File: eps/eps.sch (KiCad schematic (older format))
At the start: 10 parts, among them Q18 IRLZ44N, U4 STM32F411CEUx, U5 LTC4365TS8

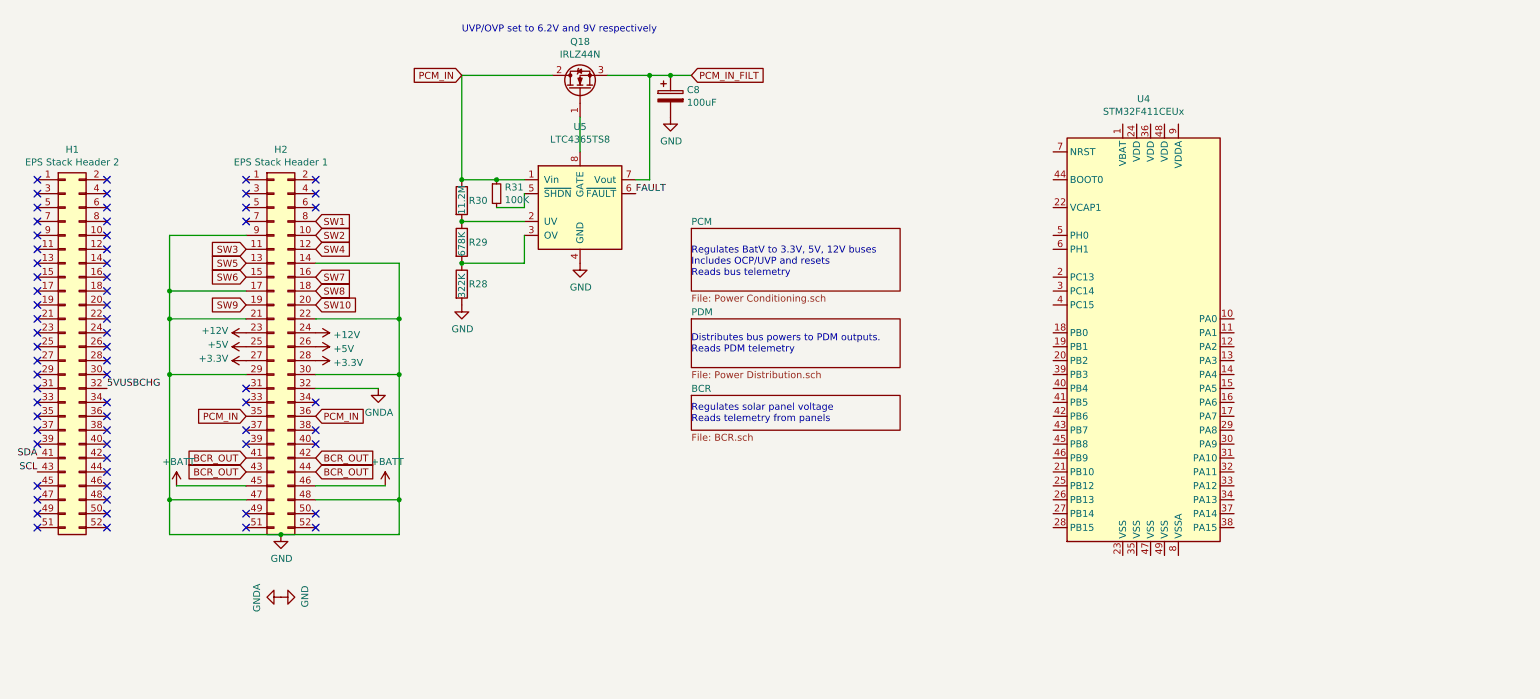
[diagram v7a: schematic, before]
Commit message: current limiters
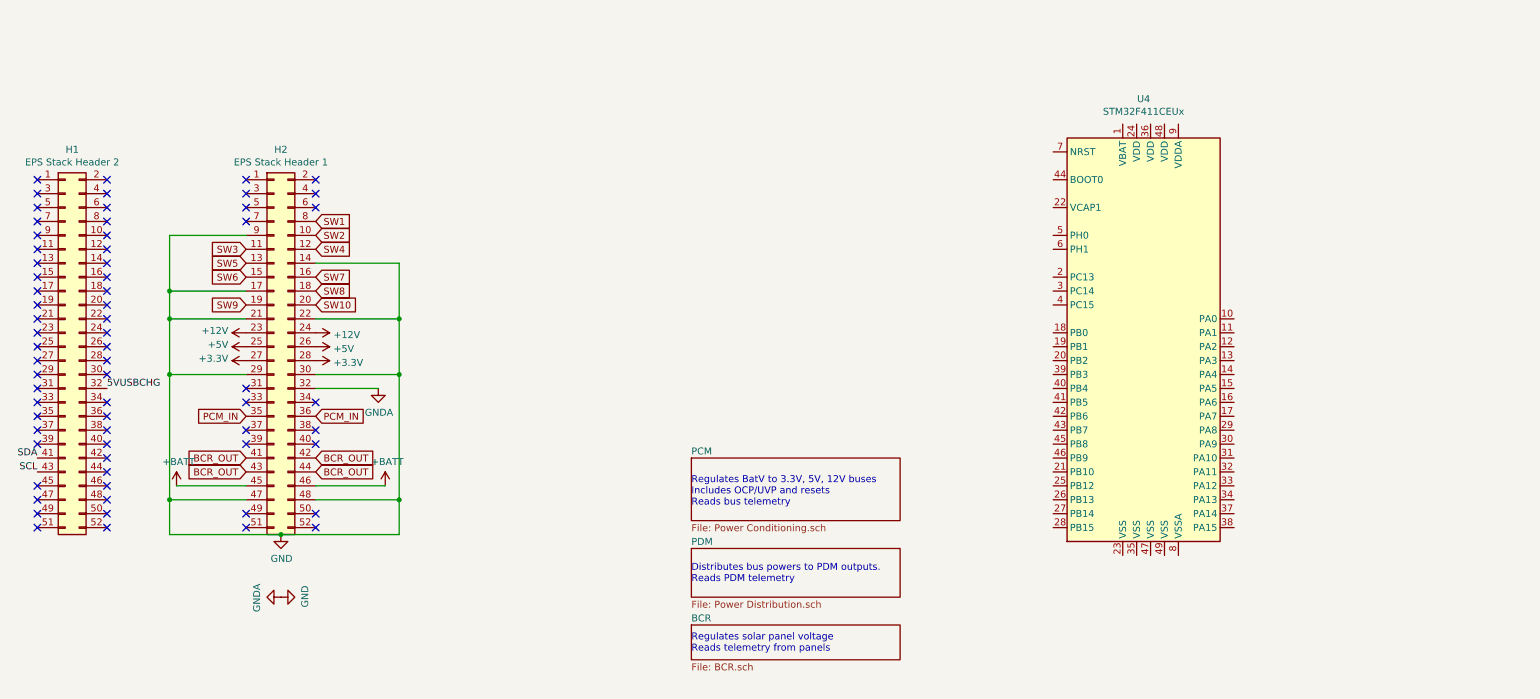
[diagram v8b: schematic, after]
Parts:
- removed C8: 100uF, symbol Device:CP
- removed Q18: IRLZ44N, Package_TO_SOT_THT:TO-220-3_Vertical, symbol Transistor_FET:IRLZ44N
- removed R28: 322K, symbol Device:R
- removed R29: 678K, symbol Device:R
- removed R30: 11.2M, symbol Device:R
- removed R31: 100K, symbol Device:R_Small
- removed U5: LTC4365TS8, symbol Power_Management:LTC4365TS8
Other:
- note removed: "UVP/OVP set to 6.2V and 9V respectively"
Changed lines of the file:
@@
 $EndComp
 $Sheet
-S 5450 2000 1500 450
+S 5450 3650 1500 450
 U 619279C9
 F0 "PCM" 50
@@
 $EndSheet
 $Sheet
-S 5450 2650 1500 350
+S 5450 4300 1500 350
 U 61928B56
 F0 "PDM" 50
@@
 $EndSheet
 $Sheet
-S 5450 3200 1500 250
+S 5450 4850 1500 250
 U 61929CC0
 F0 "BCR" 50
@@
 Text GLabel 2750 1950 2    50   Input ~ 0
 SW1
-Text Notes 5450 2350 0    50   ~ 0
+Text Notes 5450 4000 0    50   ~ 0
 Regulates BatV to 3.3V, 5V, 12V buses\nIncludes OCP/UVP and resets\nReads bus telemetry
-Text Notes 5450 2900 0    50   ~ 0
+Text Notes 5450 4550 0    50   ~ 0
 Distributes bus powers to PDM outputs. \nReads PDM telemetry\n
-Text Notes 5450 3400 0    50   ~ 0
+Text Notes 5450 5050 0    50   ~ 0
 Regulates solar panel voltage\nReads telemetry from panels\n
 $Comp
@@
 	1    0    0    -1
 $EndComp
-$Comp
-L Power_Management:LTC4365TS8 U5
-U 1 1 6180BC68
-P 4650 1850
-F 0 "U5" H 4650 2431 50  0000 C CNN
-F 1 "LTC4365TS8" H 4650 2340 50  0000 C CNN
-F 2 "" H 4350 2100 50  0001 C CNN
-F 3 "https://www.analog.com/media/en/technical-documentation/data-sheets/4365fa.pdf" H 4650 1950 50  0001 C CNN
-	1    4650 1850
-	1    0    0    -1
-$EndComp
-$Comp
-L Transistor_FET:IRLZ44N Q18
-U 1 1 6180D601
-P 4650 1000
-F 0 "Q18" V 4992 1000 50  0000 C CNN
-F 1 "IRLZ44N" V 4901 1000 50  0000 C CNN
-F 2 "Package_TO_SOT_THT:TO-220-3_Vertical" H 4900 925 50  0001 L CIN
-F 3 "http://www.irf.com/product-info/datasheets/data/irlz44n.pdf" H 4650 1000 50  0001 L CNN
-	1    4650 1000
-	0    -1   -1   0
-$EndComp
-Wire Wire Line
-	4650 1450 4650 1200
-Text GLabel 3800 900  0    50   Input ~ 0
-PCM_IN
-Wire Wire Line
-	3800 1650 3800 900
-Wire Wire Line
-	4850 900  5150 900
-Wire Wire Line
-	5050 1650 5150 1650
-Wire Wire Line
-	5150 1650 5150 900
-Text GLabel 5450 900  2    50   Input ~ 0
-PCM_IN_FILT
-Wire Wire Line
-	5150 900  5300 900
-Connection ~ 5150 900
-$Comp
-L Device:CP C8
-U 1 1 618175DC
-P 5300 1050
-F 0 "C8" H 5418 1096 50  0000 L CNN
-F 1 "100uF" H 5418 1005 50  0000 L CNN
-F 2 "" H 5338 900 50  0001 C CNN
-F 3 "~" H 5300 1050 50  0001 C CNN
-	1    5300 1050
-	1    0    0    -1
-$EndComp
-Connection ~ 5300 900
-Wire Wire Line
-	5300 900  5450 900
-$Comp
-L power:GND #PWR033
-U 1 1 6181B18B
-P 5300 1200
-F 0 "#PWR033" H 5300 950 50  0001 C CNN
-F 1 "GND" H 5305 1027 50  0000 C CNN
-F 2 "" H 5300 1200 50  0001 C CNN
-F 3 "" H 5300 1200 50  0001 C CNN
-	1    5300 1200
-	1    0    0    -1
-$EndComp
-$Comp
-L Device:R R28
-U 1 1 6181BFCB
-P 3800 2400
-F 0 "R28" H 3850 2400 50  0000 L CNN
-F 1 "322K" V 3800 2300 50  0000 L CNN
-F 2 "" V 3730 2400 50  0001 C CNN
-F 3 "~" H 3800 2400 50  0001 C CNN
-	1    3800 2400
-	1    0    0    -1
-$EndComp
-$Comp
-L Device:R R29
-U 1 1 6181C3B8
-P 3800 2100
-F 0 "R29" H 3850 2100 50  0000 L CNN
-F 1 "678K" V 3800 2000 50  0000 L CNN
-F 2 "" V 3730 2100 50  0001 C CNN
-F 3 "~" H 3800 2100 50  0001 C CNN
-	1    3800 2100
-	1    0    0    -1
-$EndComp
-$Comp
-L Device:R R30
-U 1 1 6181CB56
-P 3800 1800
-F 0 "R30" H 3850 1800 50  0000 L CNN
-F 1 "11.2M" V 3800 1700 50  0000 L CNN
-F 2 "" V 3730 1800 50  0001 C CNN
-F 3 "~" H 3800 1800 50  0001 C CNN
-	1    3800 1800
-	1    0    0    -1
-$EndComp
-Wire Wire Line
-	4250 2050 4250 2250
-$Comp
-L Device:R_Small R31
-U 1 1 6181F3F7
-P 4050 1750
-F 0 "R31" H 4109 1796 50  0000 L CNN
-F 1 "100K" H 4109 1705 50  0000 L CNN
-F 2 "" H 4050 1750 50  0001 C CNN
-F 3 "~" H 4050 1750 50  0001 C CNN
-	1    4050 1750
-	1    0    0    -1
-$EndComp
-Wire Wire Line
-	3800 900  4450 900
-Connection ~ 4050 1650
-Wire Wire Line
-	4050 1650 4250 1650
-Wire Wire Line
-	4250 1750 4250 1850
-Wire Wire Line
-	4250 1850 4050 1850
-Wire Wire Line
-	3800 1650 4050 1650
-Connection ~ 3800 1650
-Wire Wire Line
-	3800 1950 4250 1950
-Connection ~ 3800 1950
-Wire Wire Line
-	3800 2250 4250 2250
-Connection ~ 3800 2250
-$Comp
-L power:GND #PWR?
-U 1 1 61826AE0
-P 4650 2250
-F 0 "#PWR?" H 4650 2000 50  0001 C CNN
-F 1 "GND" H 4655 2077 50  0000 C CNN
-F 2 "" H 4650 2250 50  0001 C CNN
-F 3 "" H 4650 2250 50  0001 C CNN
-	1    4650 2250
-	1    0    0    -1
-$EndComp
-$Comp
-L power:GND #PWR?
-U 1 1 618271F0
-P 3800 2550
-F 0 "#PWR?" H 3800 2300 50  0001 C CNN
-F 1 "GND" H 3805 2377 50  0000 C CNN
-F 2 "" H 3800 2550 50  0001 C CNN
-F 3 "" H 3800 2550 50  0001 C CNN
-	1    3800 2550
-	1    0    0    -1
-$EndComp
-Text Label 5050 1750 0    50   ~ 0
-FAULT
-Text Notes 3800 600  0    50   ~ 0
-UVP/OVP set to 6.2V and 9V respectively
 $EndSCHEMATC
